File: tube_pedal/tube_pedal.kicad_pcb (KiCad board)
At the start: 2 copper layers, 78.5 x 56.1 mm, 35 parts, among them J1 Conn_01x01_Socket, J2 Conn_01x01_Socket, J3 Conn_01x01_Socket, J4 Conn_01x01_Socket, J5 Conn_01x01_Socket, J6 Conn_01x01_Socket, Q1 BC328, Q2 BC328, Q3 BC328, U1 JAN6418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

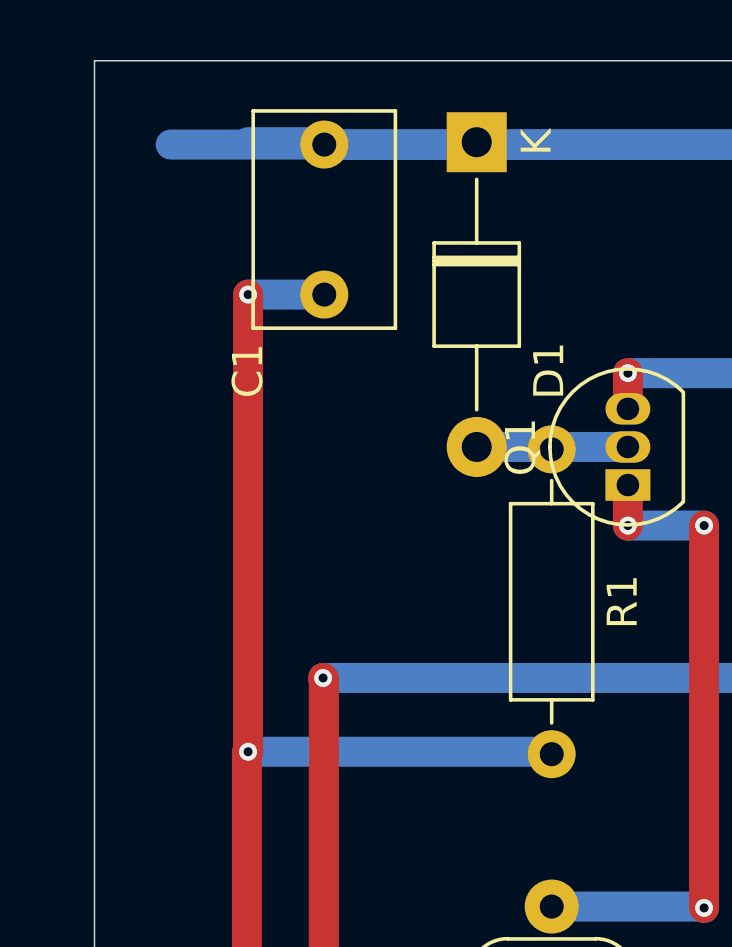
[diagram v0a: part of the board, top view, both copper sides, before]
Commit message: Changed voltage cap.
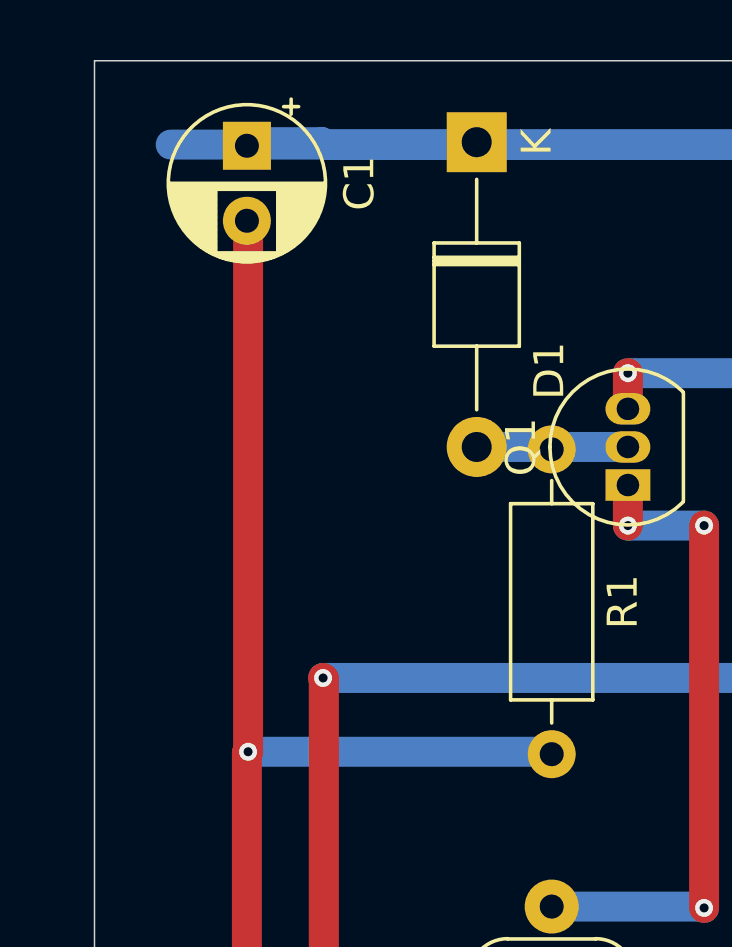
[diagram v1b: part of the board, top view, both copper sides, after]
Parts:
- C1: value 1uF -> 10uF; footprint Capacitor_THT:C_Rect_L7.0mm_W4.5mm_P5.00mm -> Capacitor_THT:CP_Radial_D5.0mm_P2.50mm
- moved C1 2.58 mm to (81.3, 40.7)
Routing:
- net GND: vias 15 -> 14

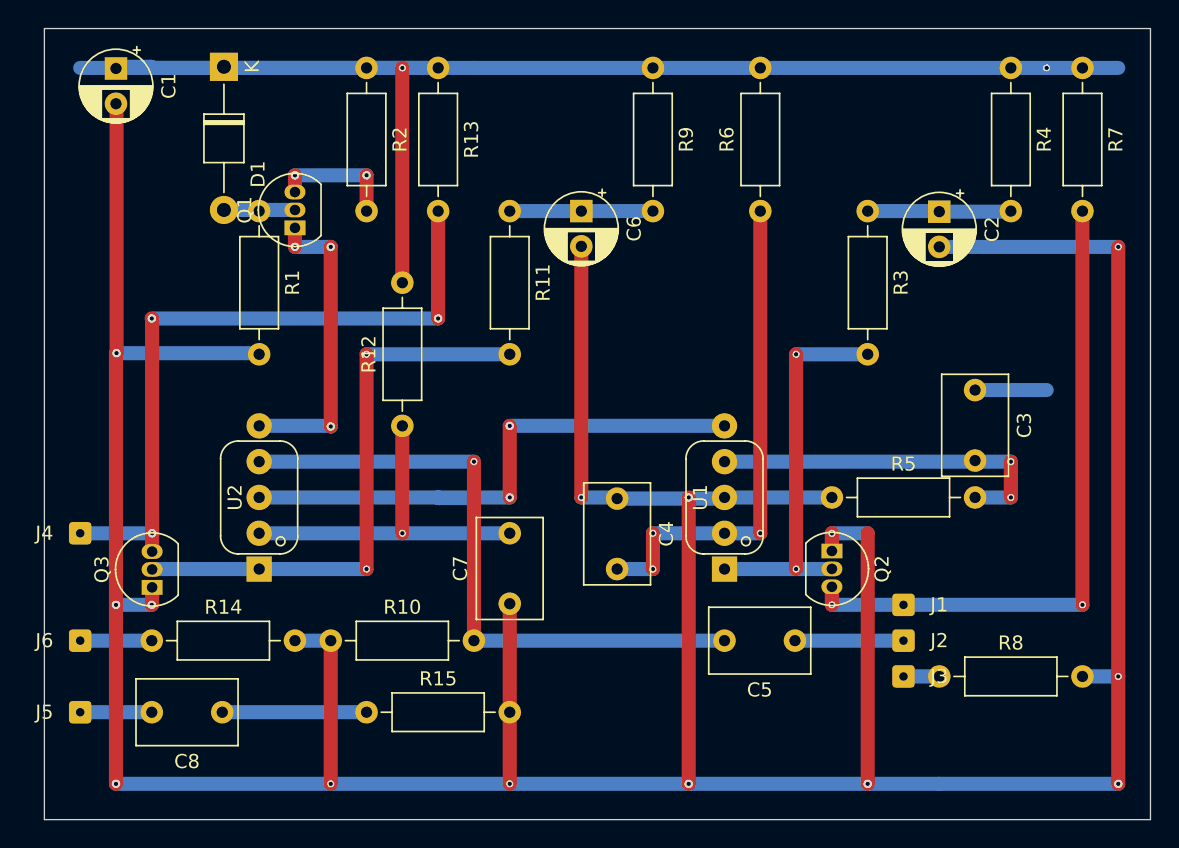
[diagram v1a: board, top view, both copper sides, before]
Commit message: Updated grid origin.
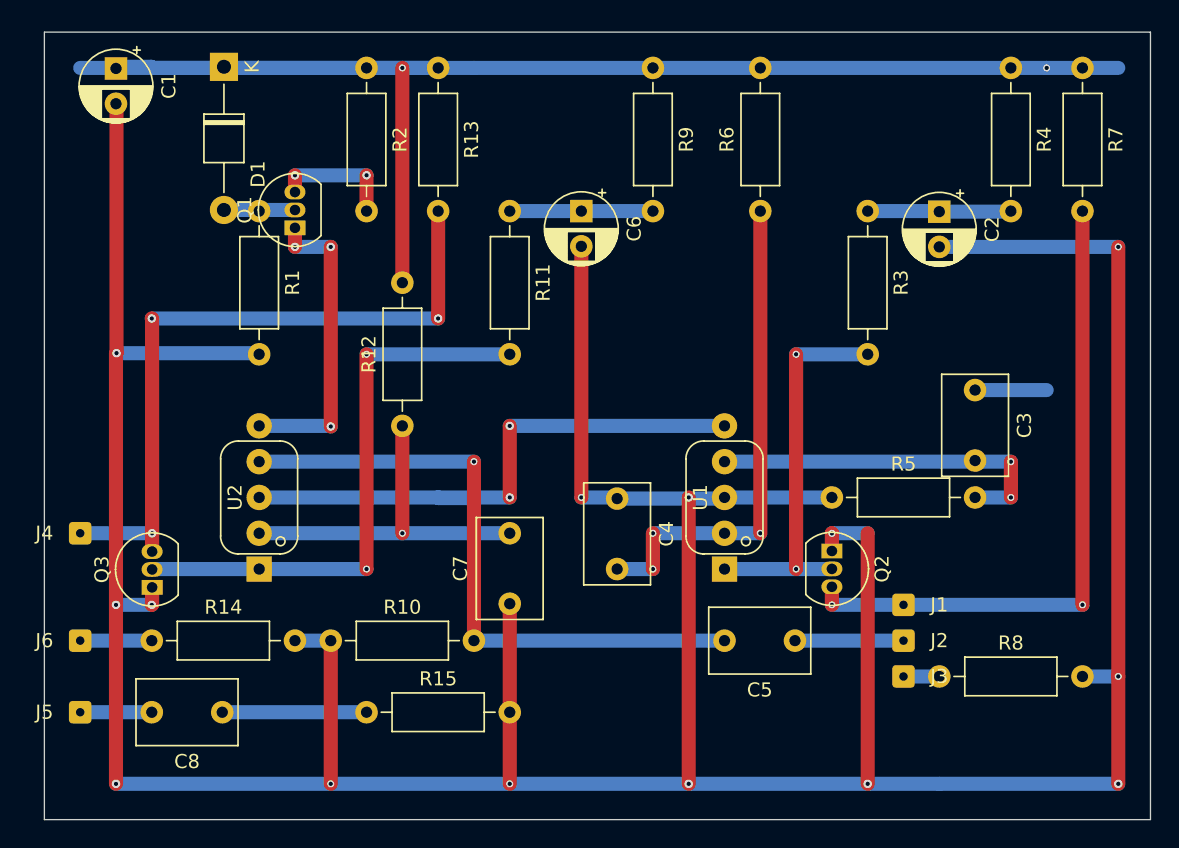
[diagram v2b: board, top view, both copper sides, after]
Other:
- board size 78.5 x 56.1 mm -> 78.5 x 55.9 mm
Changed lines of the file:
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@@
 		(pad_to_mask_clearance 0)
 		(allow_soldermask_bridges_in_footprints no)
+		(grid_origin 76.2 38.1)
 		(pcbplotparams
 			(layerselection 0x00010fc_ffffffff)
@@
 	)
 	(gr_line
-		(start 76.2 37.846)
-		(end 154.686 37.846)
+		(start 76.2 38.1)
+		(end 154.686 38.1)
 		(stroke
 			(width 0.05)
@@
 	)
 	(gr_line
-		(start 154.686 37.846)
+		(start 154.686 38.1)
 		(end 154.686 93.98)
 		(stroke
@@
 	(gr_line
 		(start 76.2 93.98)
-		(end 76.2 37.846)
+		(end 76.2 38.1)
 		(stroke
 			(width 0.05)
@@
 	)
 	(gr_text "15"
-		(at 114.3 35.56 0)
+		(at 114.3 38.1 0)
 		(layer "Cmts.User")
 		(effects
@@
 	)
 	(gr_text "5"
-		(at 88.9 35.56 0)
+		(at 88.9 38.1 0)
 		(layer "Cmts.User")
 		(effects
@@
 	)
 	(gr_text "25"
-		(at 139.7 35.56 0)
+		(at 139.7 38.1 0)
 		(layer "Cmts.User")
 		(effects
@@
 	)
 	(gr_text "20"
-		(at 127.254 35.56 0)
+		(at 127.254 38.1 0)
 		(layer "Cmts.User")
 		(effects
@@
 	)
 	(gr_text "29"
-		(at 150.114 35.56 0)
+		(at 150.114 38.1 0)
 		(layer "Cmts.User")
 		(effects
@@
 	)
 	(gr_text "10"
-		(at 101.854 35.56 0)
+		(at 101.854 38.1 0)
 		(layer "Cmts.User")
 		(effects
@@
 	)
 	(gr_text "1"
-		(at 78.74 35.56 0)
+		(at 78.74 38.1 0)
 		(layer "Cmts.User")
 		(effects

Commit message: Minor changes.
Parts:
- moved J4 2.54 mm to (81.3, 73.7)
- moved J5 2.54 mm to (81.3, 86.4)
- moved J6 2.54 mm to (81.3, 81.3)
- moved C1 2.54 mm to (83.8, 40.7)
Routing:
- net GND: track 289.9 -> 302.6 mm, vias 14 -> 15
- net Net-(J6-Pin_1): track 5.08 -> 2.54 mm
- net Net-(J5-Pin_1): track 5.08 -> 2.54 mm
- net Net-(J4-Pin_1): track 49.6 -> 47.1 mm
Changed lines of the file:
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@@
 		(tags "to-92 sc-43 sc-43a sot54 PA33 transistor")
 		(property "Reference" "Q3"
-			(at 1.27 -3.56 90)
+			(at 1.27 -2.56416 90)
 			(layer "F.SilkS")
 			(effects
@@
 	(footprint "Connector_Wire:SolderWire-0.1sqmm_1x01_D0.4mm_OD1mm"
 		(layer "F.Cu")
-		(at 78.74 86.36)
+		(at 81.28 86.36)
 		(descr "Soldered wire connection, for a single 0.1 mm² wire, basic insulation, conductor diameter 0.4mm, outer diameter 1mm, size source Multi-Contact FLEXI-E 0.1 (https://ec.staubli.com/AcroFiles/Catalogues/TM_Cab-Main-11014119_(en)_hi.pdf), bend radius 3 times outer diameter, generated with kicad-footprint-generator")
 		(tags "connector wire 0.1sqmm")
@@
 	(footprint "Connector_Wire:SolderWire-0.1sqmm_1x01_D0.4mm_OD1mm"
 		(layer "F.Cu")
-		(at 78.74 73.66)
+		(at 81.28 73.66)
 		(descr "Soldered wire connection, for a single 0.1 mm² wire, basic insulation, conductor diameter 0.4mm, outer diameter 1mm, size source Multi-Contact FLEXI-E 0.1 (https://ec.staubli.com/AcroFiles/Catalogues/TM_Cab-Main-11014119_(en)_hi.pdf), bend radius 3 times outer diameter, generated with kicad-footprint-generator")
 		(tags "connector wire 0.1sqmm")
@@
 	(footprint "Connector_Wire:SolderWire-0.1sqmm_1x01_D0.4mm_OD1mm"
 		(layer "F.Cu")
-		(at 78.74 81.28)
+		(at 81.28 81.28)
 		(descr "Soldered wire connection, for a single 0.1 mm² wire, basic insulation, conductor diameter 0.4mm, outer diameter 1mm, size source Multi-Contact FLEXI-E 0.1 (https://ec.staubli.com/AcroFiles/Catalogues/TM_Cab-Main-11014119_(en)_hi.pdf), bend radius 3 times outer diameter, generated with kicad-footprint-generator")
 		(tags "connector wire 0.1sqmm")
@@
 	(footprint "Capacitor_THT:CP_Radial_D5.0mm_P2.50mm"
 		(layer "F.Cu")
-		(at 81.28 40.68 -90)
+		(at 83.82 40.68 -90)
 		(descr "CP, Radial series, Radial, pin pitch=2.50mm, , diameter=5mm, Electrolytic Capacitor")
 		(tags "CP Radial series Radial pin pitch 2.50mm  diameter 5mm Electrolytic Capacitor")
@@
 	)
 	(segment
-		(start 81.28 78.74)
-		(end 81.28 60.92)
+		(start 83.84416 77.498746)
+		(end 83.84416 78.71584)
 		(width 1)
 		(layer "F.Cu")
@@
 	)
 	(segment
-		(start 81.32 43.22)
-		(end 81.32 60.88)
+		(start 78.74 78.74)
+		(end 78.74 91.44)
 		(width 1)
 		(layer "F.Cu")
@@
 	)
 	(segment
-		(start 83.84416 77.498746)
-		(end 83.84416 78.71584)
+		(start 78.74 43.18)
+		(end 78.74 60.88)
 		(width 1)
 		(layer "F.Cu")
@@
 	)
 	(segment
-		(start 81.28 60.92)
-		(end 81.32 60.88)
+		(start 121.92 71.12)
+		(end 121.92 91.44)
 		(width 1)
 		(layer "F.Cu")
@@
 	)
 	(segment
-		(start 121.92 71.12)
-		(end 121.92 91.44)
+		(start 83.84416 78.71584)
+		(end 83.82 78.74)
 		(width 1)
 		(layer "F.Cu")
@@
 	)
 	(segment
-		(start 83.84416 78.71584)
-		(end 83.82 78.74)
+		(start 78.74 60.88)
+		(end 78.74 78.74)
 		(width 1)
 		(layer "F.Cu")
@@
 	)
 	(segment
-		(start 81.28 43.18)
-		(end 81.32 43.22)
-		(width 1)
-		(layer "F.Cu")
-		(net 2)
-	)
-	(segment
 		(start 96.52 91.44)
 		(end 96.52 81.28)
@@
 	)
 	(segment
-		(start 81.28 91.44)
-		(end 81.28 78.74)
-		(width 1)
-		(layer "F.Cu")
-		(net 2)
-	)
-	(segment
 		(start 132.08 74.918829)
 		(end 132.08 73.668885)
@@
 	)
 	(via
-		(at 81.32 60.88)
+		(at 78.74 60.88)
 		(size 0.6)
 		(drill 0.3)
@@
 	)
 	(via
-		(at 81.28 78.74)
+		(at 78.74 78.74)
+		(size 0.6)
+		(drill 0.3)
+		(layers "F.Cu" "B.Cu")
+		(net 2)
+	)
+	(via
+		(at 78.74 43.18)
 		(size 0.6)
 		(drill 0.3)
@@
 	)
 	(via
-		(at 81.28 91.44)
+		(at 78.74 91.44)
 		(size 0.6)
 		(drill 0.3)
@@
 	)
 	(segment
-		(start 124.46 71.12)
-		(end 132.08 71.12)
+		(start 83.82 78.74)
+		(end 78.74 78.74)
 		(width 1)
 		(layer "B.Cu")
@@
 	)
 	(segment
-		(start 149.86 83.82)
-		(end 152.4 83.82)
+		(start 124.46 71.12)
+		(end 132.08 71.12)
 		(width 1)
 		(layer "B.Cu")
@@
 	)
 	(segment
-		(start 91.44 60.96)
-		(end 91.36 60.88)
+		(start 149.86 83.82)
+		(end 152.4 83.82)
 		(width 1)
 		(layer "B.Cu")
@@
 	)
 	(segment
-		(start 83.82 78.74)
-		(end 81.28 78.74)
+		(start 121.92 91.44)
+		(end 134.62 91.44)
 		(width 1)
 		(layer "B.Cu")
@@
 	)
 	(segment
-		(start 121.92 91.44)
-		(end 134.62 91.44)
+		(start 78.74 91.44)
+		(end 121.92 91.44)
 		(width 1)
 		(layer "B.Cu")
@@
 	)
 	(segment
-		(start 81.28 91.44)
-		(end 121.92 91.44)
+		(start 83.82 43.18)
+		(end 78.74 43.18)
 		(width 1)
 		(layer "B.Cu")
@@
 	)
 	(segment
-		(start 91.36 60.88)
-		(end 81.32 60.88)
-		(width 1)
-		(layer "B.Cu")
-		(net 2)
-	)
-	(segment
 		(start 116.795 71.165)
 		(end 116.84 71.12)
@@
 	)
 	(segment
+		(start 91.36 60.88)
+		(end 91.44 60.96)
+		(width 1)
+		(layer "B.Cu")
+		(net 2)
+	)
+	(segment
+		(start 78.74 60.88)
+		(end 91.36 60.88)
+		(width 1)
+		(layer "B.Cu")
+		(net 2)
+	)
+	(segment
 		(start 132.08 73.668885)
 		(end 132.088885 73.66)
@@
 	(segment
 		(start 83.82 86.36)
-		(end 78.74 86.36)
+		(end 81.28 86.36)
 		(width 1)
 		(layer "B.Cu")
@@
 	)
 	(segment
-		(start 78.74 73.66)
-		(end 83.84416 73.66)
+		(start 83.84416 73.66)
+		(end 81.28 73.66)
 		(width 1)
 		(layer "B.Cu")
@@
 	)
 	(segment
-		(start 78.74 81.28)
-		(end 83.82 81.28)
+		(start 83.82 81.28)
+		(end 81.28 81.28)
 		(width 1)
 		(layer "B.Cu")
